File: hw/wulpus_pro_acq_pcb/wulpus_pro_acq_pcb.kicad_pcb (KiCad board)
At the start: 6 copper layers, 81.1 x 38 mm, 216 parts, among them J1 DF40C-40DS-0.4V(51), J10 U.FL-R-SMT-1(10), J11 U.FL-R-SMT-1(10), J12 DF40HC(3.0)-50DS-0.4V(51), J13 Solder Jumper, J2 DF40C-40DS-0.4V(51), J3 91931-31169LF, J4 DF52-16S-0.8H(21), J5 91931-31169LF, J6 DF52-16S-0.8H(21), J7 Solder Jumper, J8 Solder Jumper, J9 Solder Jumper, M1 Mounting Hole, M2 Mounting Hole, M3 Mounting Hole, M4 Mounting Hole, Q1 NX7002BKMBYL, U1 AD8338ACPZ-R7, U10 OPA836IDBVT, U11 HV2707T-C/R8X, U12 TPS22916CYFPR, U13 MD0100, U14 MSP430FR5043IRGCT, U15 LT3463EDD#PBF, U16 TPS22916CYFPR, U17 SN74AVC4T774RSVR, U18 SN74AVC4T774RSVR, U2 OPA836IDBVT, U3 TPL0501-100RSER, U4 TS5A3159AYZPR, U5 LTC5507ES6#TRMPBF, U6 TPS22916CYFPR, U7 TS5A3159AYZPR, U8 TPS22916CYFPR, U9 IXDD604D2TR, X1 68000-106HLF, X2 FY0800018, X3 68000-106HLF, X4 68000-106HLF, X5 68000-102HLF, X6 68000-102HLF, X7 68000-102HLF, X8 68000-102HLF, Y1 AWSCR-8.00CV-T, Y2 ABS05-32.768KHZ-9-T

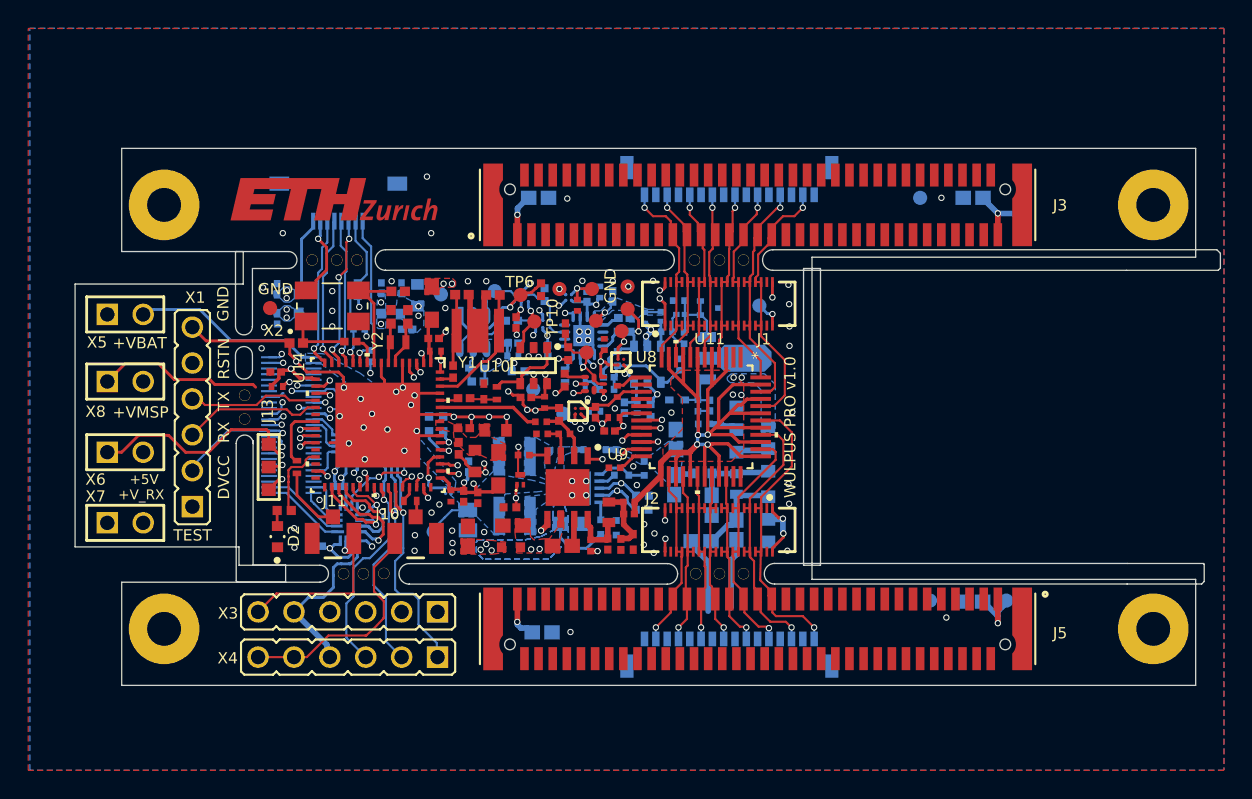
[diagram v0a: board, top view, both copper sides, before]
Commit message: Cleaned teh project, removen eval board components
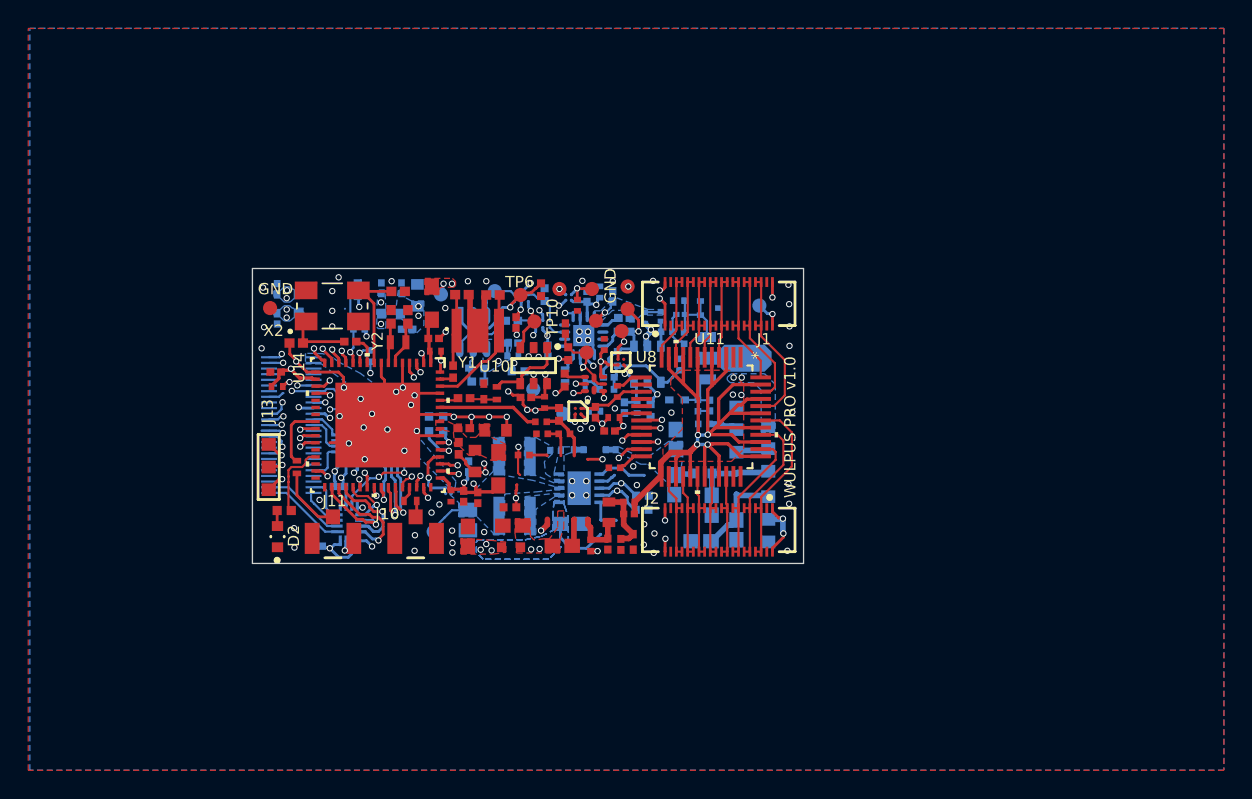
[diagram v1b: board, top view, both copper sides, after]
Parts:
- removed ? (x14): , 
- removed A1: Logo ETH Zurich, Vault:eth-zurich_3mm
- removed C34, C35, C36, C37: 2.2 uF 50V, Vault:FP-GRM188-0_2-IPC_B
- removed J3, J5: 91931-31169LF, cmut_conn:FRAMETOME_91931-31169LF
- removed J4, J6: DF52-16S-0.8H(21), wulpus_hv:CONN_DF52-16S-0.8H(21)_HIR
- removed M1, M2, M3, M4: Mounting Hole, Vault:Mounting Hole
- removed PJ1: 5051100892, wulpus:MOLEX_5051100892
- removed Q1: NX7002BKMBYL, SamacSys:NX7002BKMBYL
- removed R24: 3k 1/3W, SamacSys:ERJP03_PA3_(0603)
- removed R39, R42: 1MΩ, SamacSys:ERJ2RKD1004X
- removed R40: 43.2 kΩ, SamacSys:ERJ2RKD1004X
- removed R41: 41.2 kΩ, SamacSys:ERJ2RKD1004X
- removed TP14, TP15, TP16, TP17: TP-SM-C-100, wulpus:TP-SM-C-100
- removed U9: IXDD604D2TR, SamacSys:SON95P500X400X100-9N
- removed X1, X3, X4: 68000-106HLF, Vault:68000-106HLF
- removed X5, X6, X7, X8: 68000-102HLF, Vault:68000-102HLF
- U13: value MD0100 -> MD0100N8-G
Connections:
- net AVCC1 renamed /U_msp430/AVCC1
- net BOT_EL renamed /U_hv_mux_tr_sw/BOT_EL
- net BUF_OUT renamed /U_rx_path_lp_filter/BUF_OUT
- net CH0_IN renamed /U_msp430/CH0_IN
- net CH0_OUT renamed /U_msp430/CH0_OUT
- net CH1_OUT renamed /U_msp430/CH1_OUT
- net CH_0 renamed /U_hv_mux_tr_sw/CH_0
- net CH_1 renamed /U_hv_mux_tr_sw/CH_1
- net CH_10 renamed /U_hv_mux_tr_sw/CH_10
- net CH_11 renamed /U_hv_mux_tr_sw/CH_11
- net CH_12 renamed /U_hv_mux_tr_sw/CH_12
- net CH_13 renamed /U_hv_mux_tr_sw/CH_13
- net CH_14 renamed /U_hv_mux_tr_sw/CH_14
- net CH_15 renamed /U_hv_mux_tr_sw/CH_15
- net CH_2 renamed /U_hv_mux_tr_sw/CH_2
- net CH_3 renamed /U_hv_mux_tr_sw/CH_3
- net CH_4 renamed /U_hv_mux_tr_sw/CH_4
- net CH_5 renamed /U_hv_mux_tr_sw/CH_5
- net CH_6 renamed /U_hv_mux_tr_sw/CH_6
- net CH_7 renamed /U_hv_mux_tr_sw/CH_7
- net CH_8 renamed /U_hv_mux_tr_sw/CH_8
- net CH_9 renamed /U_hv_mux_tr_sw/CH_9
- net DATA_READY renamed /U_host_connector/HOST_DATA_RDY
- net DVCC1 renamed +VCC_MSP430
- net ENV_DET_EN renamed /U_msp430/ENV_DET_EN
- net ENV_OUT renamed /U_rx_path/ENV_OUT
- net FILTER_SHDN_N renamed /U_msp430/LP_FILT_EN
- net HFXIN renamed /U_msp430/HFXIN
- net HFXOUT renamed /U_msp430/HFXOUT
- net HOST_LINK_RDY renamed /U_host_connector/HOST_LINK_RDY
- net HOST_SPARE renamed /U_host_connector/HOST_SPARE
- net HOST_SPI_CS renamed /U_host_connector/HOST_SPI_CS
- net HV_EN1 renamed /U_msp430/HV_POS_EN
- net HV_EN2 renamed /U_msp430/HV_NEG_EN
- net HV_MUX_CLR renamed /U_msp430/HV_MUX_CLR
- net HV_MUX_LE renamed /U_msp430/HV_MUX_LE
- net HV_MUX_PWR_EN renamed /U_msp430/HV_MUX_PWR_EN
- net HV_PWR_EN renamed /U_msp430/HV_PWR_EN
- net I2C_A_SCL renamed /U_host_connector/I2C_A_SCL
- net LED_MSP430 renamed /U_msp430/LED_MSP430
- net LFXIN renamed /U_msp430/LFXIN
- net LFXOUT renamed /U_msp430/LFXOUT
- net LVL_SHIFTER_EN renamed /U_host_connector/LVL_SHIFTER_EN
- net MSP_CS renamed /U_host_connector/MSP_CS
- net MSP_DR1 renamed /U_host_connector/MSP_DR1
- net MSP_DR2 renamed /U_host_connector/MSP_DR2
- net NetC10_2 renamed Net-(U5-RFIN)
- net NetC1_1 renamed Net-(U2-VIN-)
- net NetC25_2 renamed /U_hv_mux_tr_sw/TX_HV_PULSE_IN
- net NetC27_2 renamed /U_msp430/ADC_IN
- net NetC38_1 renamed Net-(C38-Pad1)
- net NetC3_2 renamed Net-(C3-Pad2)
- net NetC4_2 renamed Net-(U1-INMR)
- net NetC54_2 renamed Net-(X2-IN/OUT)
- net NetC57_2 renamed Net-(C57-Pad2)
- net NetC67_1 renamed Net-(U15-D2)
- net NetC67_2 renamed Net-(U15-SW2)
- net NetC6_1 renamed /U_hv_mux_tr_sw/RX_OUT
- net NetC6_2 renamed Net-(C6-Pad2)
- net NetC7_2 renamed Net-(U1-INPR)
- net NetD2_2 renamed Net-(D2-A)
- net NetJ10_1 renamed Net-(J10-SIG)
- net NetJ11_1 renamed Net-(J11-SIG)
- net NetJ13_2 renamed Net-(U18-DIR4)
- net NetJ8_2 renamed Net-(J8-Pad2)
- net NetJ9_2 renamed Net-(J9-Pad2)
- net NetL3_2 renamed Net-(U15-SW1)
- net NetR23_2 renamed Net-(U11-RGND)
- net NetR31_1 renamed Net-(U14-CH1_IN)
- net NetR4_2 renamed Net-(U1-DETO)
- net NetR5_2 renamed Net-(U3-H)
- net NetR8_2 renamed Net-(U2-VIN+)
- net NetTP10_1 renamed /U_rx_path/SIG_OUT
- net PCAP renamed /U_rx_path/PCAP
- net PREAMP_EN renamed /U_msp430/PREAMP_EN
- net PREAMP_PWR_EN renamed /U_msp430/PREAMP_PWR_EN
- net PULSER_IN_A renamed /U_tx_path/PULSER_IN_A
- net PULSER_IN_B renamed /U_tx_path/PULSER_IN_B
- net PULSER_OUT_A renamed /U_tx_path/PULSER_OUT_A
- net PULS_HIZ_EN renamed /U_msp430/PULS_HIZ_EN
- net PVCC renamed /U_msp430/PVCC
- net RF_BYPASS renamed /U_rx_path/RF_BYPASS
- net RF_IN_ENV renamed /U_rx_path/RF_IN_ENV
- net SPI_B_CLK renamed /U_host_connector/SPI_B_CLK
- net SPI_B_CS renamed /U_host_connector/SPI_B_CS
- net SPI_B_MISO renamed /U_host_connector/SPI_B_MISO
- net SPI_B_MOSI renamed /U_host_connector/SPI_B_MOSI
- net TRIG_OUT renamed /U_msp430/TRIG_OUT
- net TR_SW_IN renamed /U_hv_mux_tr_sw/TR_SW_IN
- net TX_RX renamed /U_hv_mux_tr_sw/TX_RX
- net USSXTIN renamed /U_msp430/USSXTIN
- net USSXTOUT renamed /U_msp430/USSXTOUT
- net UUPS_TRIG_IN renamed /U_msp430/UUPS_TRIG_IN
- net VGA_GAIN renamed /U_rx_path/VGA_GAIN
- net VGA_GAIN_CS renamed /U_msp430/VGA_GAIN_CS
- net VGA_GAIN_RC_EN renamed /U_msp430/VGA_GAIN_RC_EN
- net VGA_GAIN_RC_SINK renamed /U_msp430/VGA_GAIN_RC_SINK
- net VGA_IN renamed /U_rx_path/VGA_IN
- net VGA_OUT renamed /U_rx_path/VGA_OUT
- net VGA_PWR_EN renamed /U_msp430/VGA_PWR_EN
- C56 pad 1: JTAG_RESET_N -> /U_msp430/JTAG_RESET_N
- J1 pad 3: (no net) -> unconnected-(J1-Pad3)
- J1 pad 37: (no net) -> unconnected-(J1-Pad37)
- J1 pad 38: (no net) -> unconnected-(J1-Pad38)
- J1 pad 4: (no net) -> unconnected-(J1-Pad4)
- J12 pad 14: (no net) -> unconnected-(J12-Pad14)
- J12 pad 15: (no net) -> unconnected-(J12-Pad15)
- J12 pad 16: (no net) -> unconnected-(J12-Pad16)
- J12 pad 17: (no net) -> unconnected-(J12-Pad17)
- J12 pad 19: (no net) -> unconnected-(J12-Pad19)
- J12 pad 20: (no net) -> unconnected-(J12-Pad20)
- J12 pad 22: (no net) -> unconnected-(J12-Pad22)
- J12 pad 23: (no net) -> unconnected-(J12-Pad23)
- J12 pad 28: (no net) -> unconnected-(J12-Pad28)
- J12 pad 29: (no net) -> unconnected-(J12-Pad29)
- J12 pad 3: (no net) -> unconnected-(J12-Pad3)
- J12 pad 30: (no net) -> unconnected-(J12-Pad30)
- J12 pad 31: (no net) -> unconnected-(J12-Pad31)
- J12 pad 32: (no net) -> unconnected-(J12-Pad32)
- J12 pad 34: (no net) -> unconnected-(J12-Pad34)
- J12 pad 35: (no net) -> unconnected-(J12-Pad35)
- J12 pad 38: JTAG_TDO -> /U_msp430/TDO
- J12 pad 39: JTAG_TDI -> /U_msp430/TDI
- J12 pad 4: (no net) -> unconnected-(J12-Pad4)
- J12 pad 40: JTAG_TMS -> /U_msp430/TMS
- J12 pad 41: (no net) -> unconnected-(J12-Pad41)
- J12 pad 42: (no net) -> unconnected-(J12-Pad42)
- J12 pad 44: (no net) -> unconnected-(J12-Pad44)
- J12 pad 45: (no net) -> unconnected-(J12-Pad45)
- J12 pad 46: (no net) -> unconnected-(J12-Pad46)
- J12 pad 47: (no net) -> unconnected-(J12-Pad47)
- J12 pad 48: (no net) -> unconnected-(J12-Pad48)
- J12 pad 49: JTAG_TCK -> /U_msp430/TCK
- J12 pad 5: (no net) -> unconnected-(J12-Pad5)
- J12 pad 50: JTAG_RESET_N -> /U_msp430/RESET
- J12 pad 8: (no net) -> unconnected-(J12-Pad8)
- J2 pad 3: (no net) -> unconnected-(J2-Pad3)
- J2 pad 37: (no net) -> unconnected-(J2-Pad37)
- J2 pad 38: (no net) -> unconnected-(J2-Pad38)
- J2 pad 4: (no net) -> unconnected-(J2-Pad4)
- R19 pad 1: PULSER_EN_A -> /U_tx_path/PULSER_EN_A
- R19 pad 2: PULSER_EN_B -> /U_tx_path/PULSER_EN_B
- R20 pad 2: PULSER_OUT_B -> /U_tx_path/PULSER_OUT_B
- R37 pad 2: JTAG_RESET_N -> /U_msp430/JTAG_RESET_N
- R45 pad 1: JTAG_TEST -> /U_msp430/TEST
- U1 pad 10: (no net) -> unconnected-(U1-OUTM-Pad10)
- U1 pad 12: (no net) -> unconnected-(U1-FBKP-Pad12)
- U1 pad 2: (no net) -> unconnected-(U1-INPD-Pad2)
- U1 pad 3: (no net) -> unconnected-(U1-INMD-Pad3)
- U1 pad 9: (no net) -> unconnected-(U1-FBKM-Pad9)
- U11 pad 1: (no net) -> unconnected-(U11-NC-Pad1)
- U11 pad 14: (no net) -> unconnected-(U11-NC-Pad14)
- U11 pad 16: (no net) -> unconnected-(U11-VSS-Pad16)
- U11 pad 19: RX_SPI_MOSI -> /U_host_connector/MOSI
- U11 pad 2: (no net) -> unconnected-(U11-NC-Pad2)
- U11 pad 20: RX_SPI_CLK -> /U_host_connector/SCLK
- U11 pad 23: RX_SPI_MISO -> /U_host_connector/MISO
- U11 pad 35: (no net) -> unconnected-(U11-NC-Pad35)
- U11 pad 36: (no net) -> unconnected-(U11-NC-Pad36)
- U13 pad 2: (no net) -> unconnected-(U13-COM-Pad2)
- U14 pad 11: JTAG_TEST -> /U_msp430/JTAG_TEST
- U14 pad 12: JTAG_RESET_N -> /U_msp430/JTAG_RESET_N
- U14 pad 13: JTAG_TDO -> /U_msp430/JTAG_TDO
- U14 pad 14: JTAG_TDI -> /U_msp430/JTAG_TDI
- U14 pad 15: JTAG_TMS -> /U_msp430/JTAG_TMS
- U14 pad 16: JTAG_TCK -> /U_msp430/JTAG_TCK
- U14 pad 21: BSL_UART_TX -> unconnected-(U14-P2.0_UCA1CLK_UCA3SIMO_UCA3TXD-Pad21)
- U14 pad 22: BSL_UART_RX -> unconnected-(U14-P2.1_UCA1STE_UCA3SOMI_UCA3RXD-Pad22)
- U14 pad 23: (no net) -> unconnected-(U14-P1.6_UCA3STE_UCB0SIMO_UCB0SDA-Pad23)
- U14 pad 28: (no net) -> unconnected-(U14-P4.0_RTCCLK_TA4.1_MTIF_PIN_EN-Pad28)
- U14 pad 30: (no net) -> unconnected-(U14-P4.2_UCA0STE_TB0.5_UCA3SIMO_UCA3TXD-Pad30)
- U14 pad 32: (no net) -> unconnected-(U14-P4.4_UCA0SOMI_UCA0RXD-Pad32)
- U14 pad 34: HOST_SPI_MOSI -> /U_msp430/HOST_SPI_MOSI
- U14 pad 35: HOST_SPI_MISO -> /U_msp430/HOST_SPI_MISO
- U14 pad 36: HOST_SPI_CLK -> /U_msp430/HOST_SPI_CLK
- U14 pad 38: RX_SPI_CLK -> /U_msp430/RX_SPI_CLK
- U14 pad 39: RX_SPI_MOSI -> /U_msp430/RX_SPI_MOSI
- U14 pad 40: RX_SPI_MISO -> /U_msp430/RX_SPI_MISO
- U15 pad 10: NetR39_1 -> Net-(U15-FB1)
- U15 pad 6: NetR41_2 -> Net-(U15-FB2)
- U15 pad 7: NetR41_1 -> Net-(U15-VREF)
- U17 pad 10: HOST_SPI_MOSI -> /U_host_connector/HOST_SPI_MOSI
- U17 pad 11: HOST_SPI_CLK -> /U_host_connector/HOST_SPI_CLK
- U17 pad 12: HOST_SPI_MISO -> /U_host_connector/HOST_SPI_MISO
- U18 pad 10: (no net) -> unconnected-(U18-B3-Pad10)
- U18 pad 3: (no net) -> unconnected-(U18-A3-Pad3)
- U3 pad 2: RX_SPI_MOSI -> /U_host_connector/MOSI
- U3 pad 5: RX_SPI_CLK -> /U_host_connector/SCLK
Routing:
- net (no net): track 0.00 -> 146.8 mm, vias 0 -> 24
- net /U_hv_mux_tr_sw/BOT_EL: track 121.9 -> 12.7 mm, vias 12 -> 8
- net GND: track 141.5 -> 66.6 mm, vias 104 -> 96
- net RX_SPI_MOSI: track 29.8 -> 0.00 mm, vias 3 -> 0
- net RX_SPI_CLK: track 27.4 -> 0.00 mm, vias 3 -> 0
- net JTAG_RESET_N: track 26.2 -> 0.00 mm, vias 2 -> 0
- net +VCC_MSP430: track 43.9 -> 20.0 mm
- net RX_SPI_MISO: track 22.3 -> 0.00 mm, vias 2 -> 0
- net +V_RX_CONN: track 23.4 -> 1.34 mm
- net JTAG_TDO: track 18.7 -> 0.00 mm, vias 2 -> 0
- net JTAG_TDI: track 18.1 -> 0.00 mm, vias 4 -> 0
- net JTAG_TMS: track 17.6 -> 0.00 mm, vias 2 -> 0
- net HOST_SPI_MISO: track 15.0 -> 0.00 mm, vias 1 -> 0
- net +5V: track 17.3 -> 2.36 mm
- net HOST_SPI_CLK: track 14.9 -> 0.00 mm, vias 1 -> 0
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- added copper zone on In3.Cu, net /U_tx_path/PULSER_OUT_B
- removed copper zone on In3.Cu, net PULSER_OUT_B
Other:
- board size 81.1 x 38 mm -> 39 x 20.9 mm
- board text removed: "+5V"
- board text removed: "+VBAT"
- board text removed: "+VMSP"
- board text removed: "+V_RX"
- board text removed: "BOT EL"
- board text removed: "Board #"
- board text removed: "DVCC"
- board text removed: "QA"
- board text removed: "RSTN"
- board text removed: "RX"
- board text removed: "TEST"
- board text removed: "TX"
